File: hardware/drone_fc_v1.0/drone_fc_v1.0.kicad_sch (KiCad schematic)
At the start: 1 part, among them U1 nRF52832-QF48

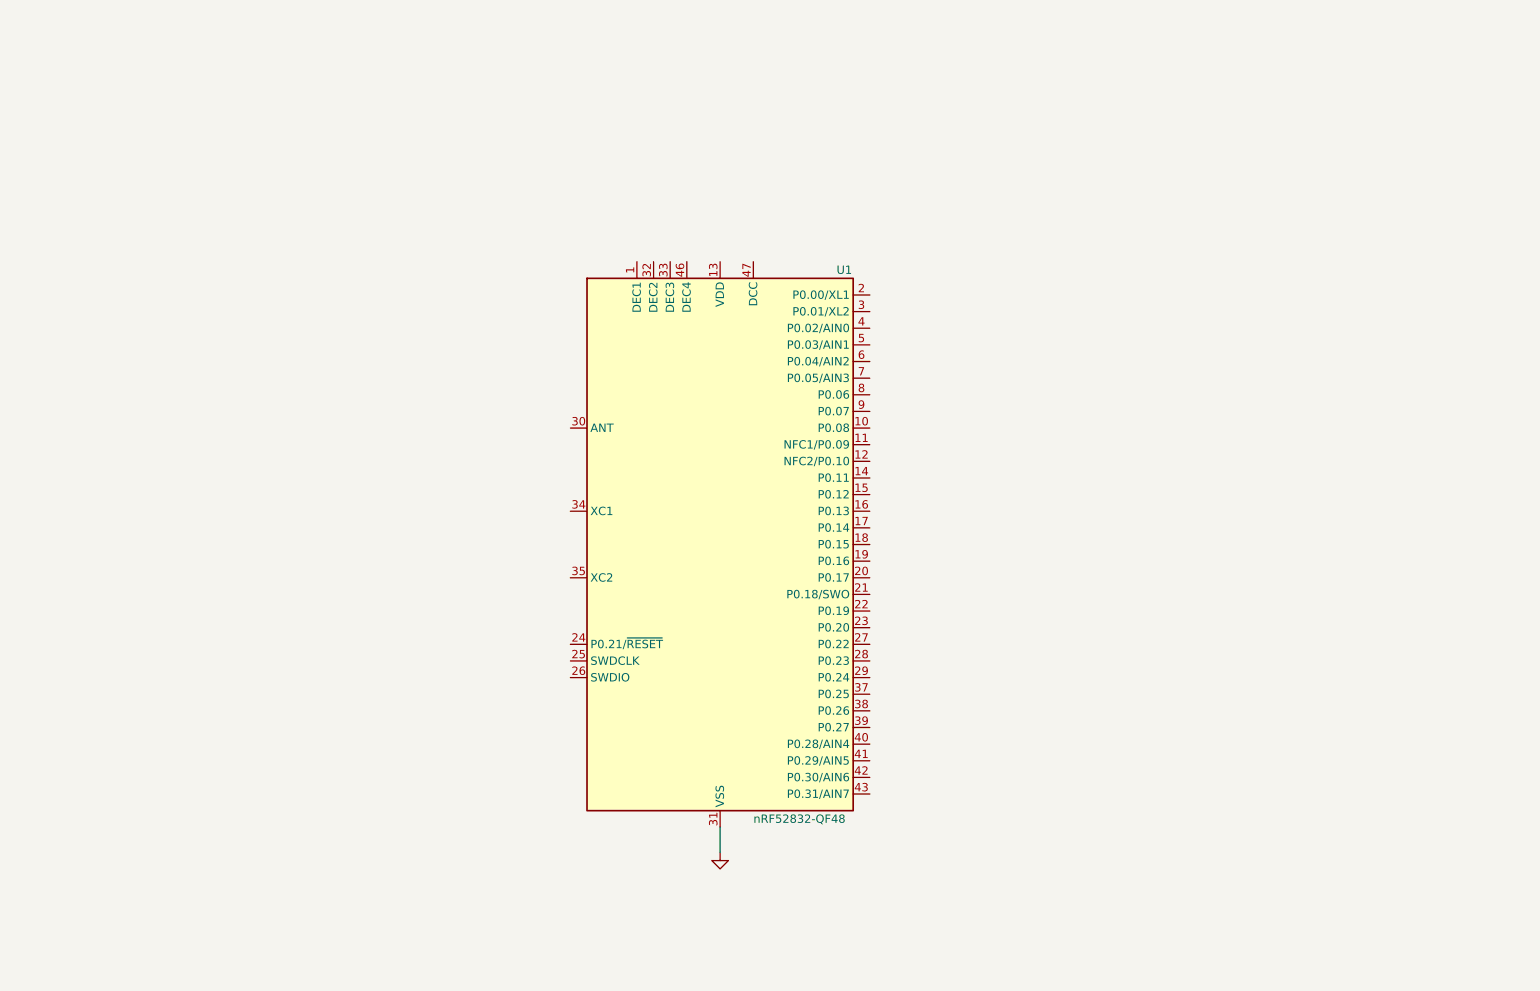
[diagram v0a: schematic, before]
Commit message: feat: initial schematic design
Completed the base schematic for the project. Major hardware blocks include:
- nRF52832 core setup (configured for internal LDO, 32MHz crystal only)
- 5V to 3.3V linear regulator for ESC power input
- 2S battery voltage divider (180k/100k) mapped to AIN
- MPU6050 IMU on I2C0 with active-low interrupt and external pull-up
- Hardware reset button with 10k pull-up resistor
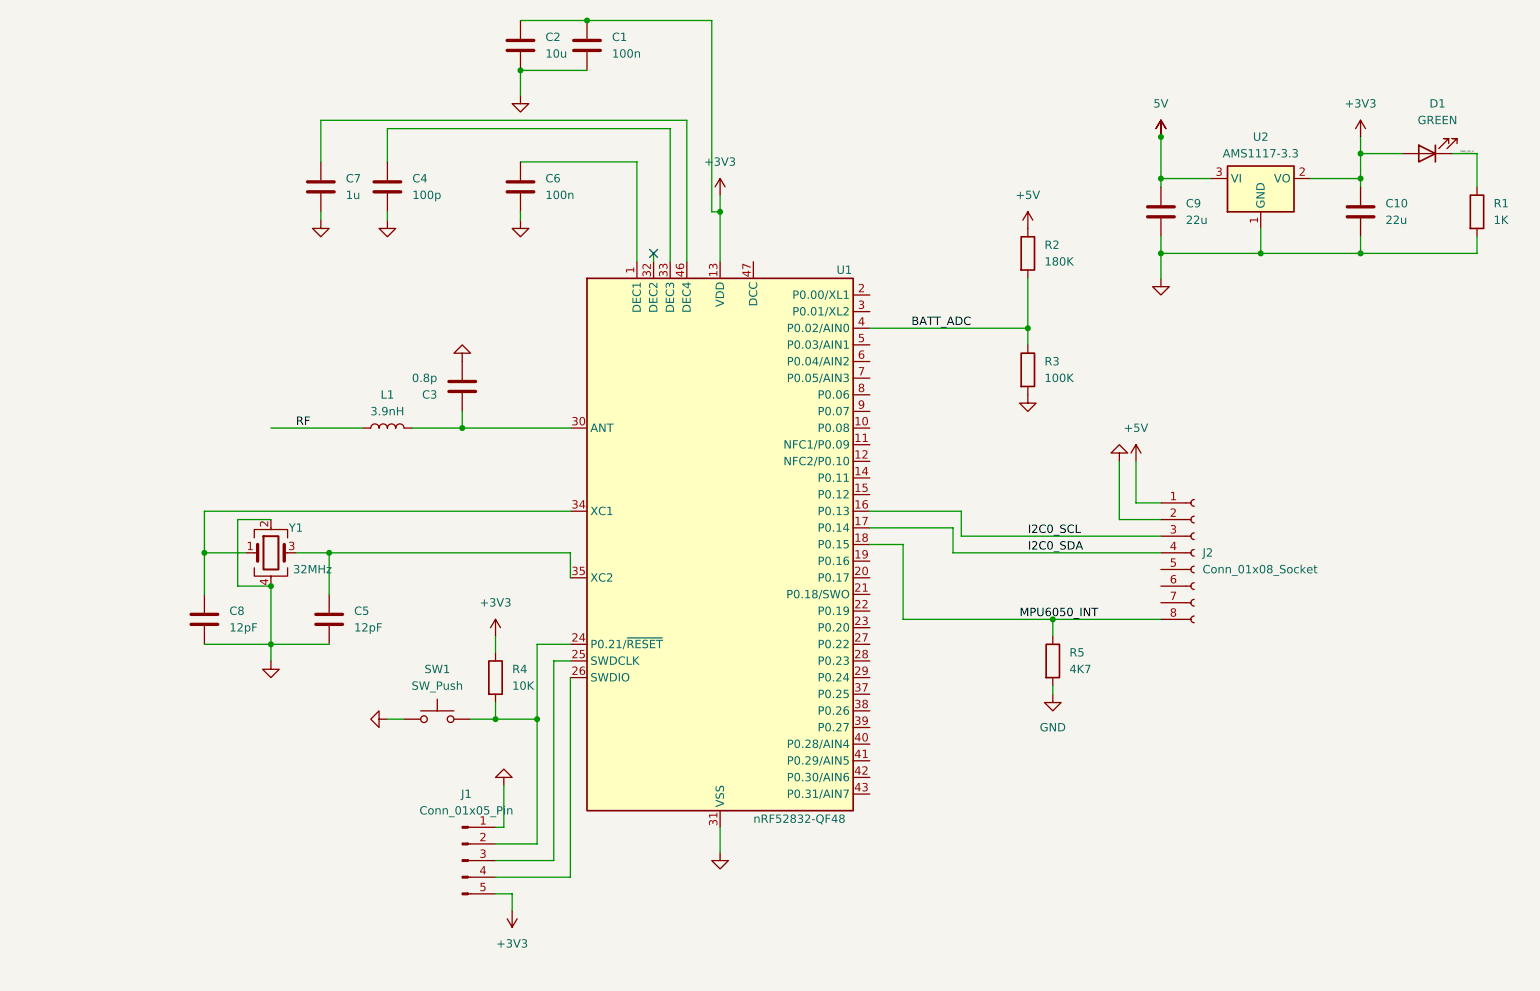
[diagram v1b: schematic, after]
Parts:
- added C1, C6: 100n, symbol Device:C
- added C10, C9: 22u, symbol Device:C
- added C2: 10u, symbol Device:C
- added C3: 0.8p, symbol Device:C
- added C4: 100p, symbol Device:C
- added C5, C8: 12pF, symbol Device:C
- added C7: 1u, symbol Device:C
- added D1: GREEN, symbol Device:LED
- added J1: Conn_01x05_Pin, symbol Connector:Conn_01x05_Pin
- added J2: Conn_01x08_Socket, symbol Connector:Conn_01x08_Socket
- added L1: 3.9nH, symbol Device:L
- added R1: 1K, symbol Device:R
- added R2: 180K, symbol Device:R
- added R3: 100K, symbol Device:R
- added R4: 10K, symbol Device:R
- added R5: 4K7, symbol Device:R
- added SW1: SW_Push, symbol Switch:SW_Push
- added U2: AMS1117-3.3, Package_TO_SOT_SMD:SOT-223-3_TabPin2, symbol Regulator_Linear:AMS1117-3.3
- added Y1: 32MHz, symbol Device:Crystal_GND24
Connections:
- net GND: now also C1.2, C10.2, C2.2, C3.1, C4.2, C5.2, C6.2, C7.2, C8.2, C9.2, J1.1 (Pin_1), J2.2 (Pin_2), R1.2, R3.2, R5.2, SW1.1, U2.1 (GND), Y1.2, Y1.4
- net at U1.1 (DEC1): now also C6.1
- net +3V3: now reaches U1.13 (VDD), U1.36 (VDD), U1.48 (VDD)
- net +3V3: now also C1.1, C10.1, C2.1, D1.2 (A), J1.5 (Pin_5), R4.1, U2.2 (VO)
- net I2C0_SCL: now reaches U1.16 (P0.13)
- net I2C0_SCL: now also J2.3 (Pin_3)
- net I2C0_SDA: now reaches U1.17 (P0.14)
- net I2C0_SDA: now also J2.4 (Pin_4)
- net MPU6050_INT: now reaches U1.18 (P0.15)
- net MPU6050_INT: now also J2.8 (Pin_8), R5.1
- net at U1.24 (P0.21/~{RESET}): now also J1.2 (Pin_2), R4.2, SW1.2
- net at U1.25 (SWDCLK): now also J1.3 (Pin_3)
- net at U1.26 (SWDIO): now also J1.4 (Pin_4)
- net at U1.30 (ANT): now also C3.2, L1.2
- net at U1.33 (DEC3): now also C4.1
- net at U1.34 (XC1): now also C8.1, Y1.1
- net at U1.35 (XC2): now also C5.1, Y1.3
- net BATT_ADC: now reaches U1.4 (P0.02/AIN0)
- net BATT_ADC: now also R2.2, R3.1
- net at U1.46 (DEC4): now also C7.1
- new net +5V: J2.1 (Pin_1), R2.1
- new net 5V: C9.1, U2.3 (VI)
- new net PWR_LED_K: D1.1 (K), R1.1
- new net RF: L1.1
- no-connect marks 0 -> 1

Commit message: feat: Finished schematics, and most of the footprinting
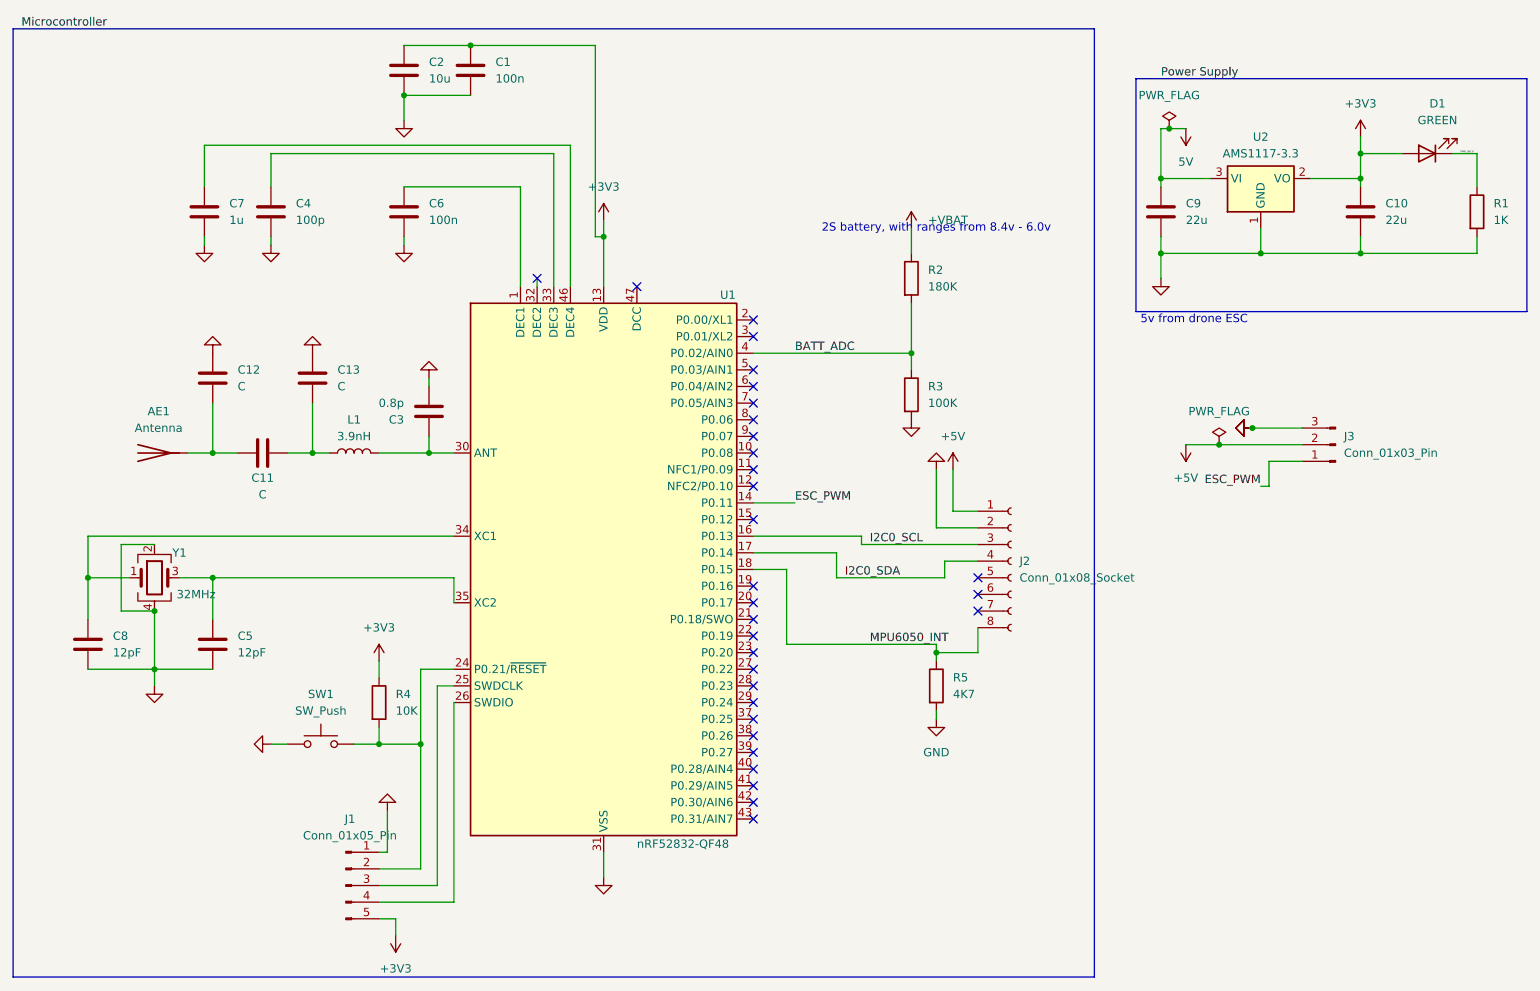
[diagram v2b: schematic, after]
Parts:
- added AE1: Antenna, RF_Antenna:Johanson_2450AT18x100, symbol Device:Antenna
- added C11, C12, C13: C, symbol Device:C
- added J3: Conn_01x03_Pin, Connector_PinHeader_2.54mm:PinHeader_1x03_P2.54mm_Vertical, symbol Connector:Conn_01x03_Pin
- C1, C3, C4, C6, C7: footprint (none) -> Capacitor_SMD:C_0402_1005Metric
- C10, C9: footprint (none) -> Capacitor_SMD:C_0805_2012Metric
- C2, C5, C8: footprint (none) -> Capacitor_SMD:C_0603_1608Metric
- D1: footprint (none) -> LED_SMD:LED_0603_1608Metric
- J1: footprint (none) -> Connector_PinHeader_2.54mm:PinHeader_1x05_P2.54mm_Vertical
- J2: footprint (none) -> Connector_PinSocket_2.54mm:PinSocket_1x08_P2.54mm_Vertical
- R1, R2, R3, R4, R5: footprint (none) -> Resistor_SMD:R_0402_1005Metric
- Y1: footprint (none) -> Crystal:Crystal_SMD_2016-4Pin_2.0x1.6mm
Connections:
- net +5V: now also J3.2 (Pin_2); no longer R2.1
- net GND: now also C12.2, C13.2, J3.3 (Pin_3)
- net ESC_PWM: now reaches U1.14 (P0.11)
- net ESC_PWM: now also J3.1 (Pin_1)
- net RF: no longer names the net of L1.1
- net RF: now also C11.2, C13.1
- new net: AE1.1 (A), C11.1, C12.1
- new net +VBAT: R2.1
- no-connect marks 1 -> 31
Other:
- note added: "2S battery, with ranges from 8.4v - 6.0v"
- note added: "5v from drone ESC"
- company: (none) -> ehuang2020
- title: (none) -> Drone Flight Controller
- moved on the sheet: C1, C2, C3, C4, C5, C6, C7, C8, J1, J2, L1, R2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
